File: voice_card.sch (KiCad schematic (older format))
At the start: 213 parts, among them J1 DDR3-DIMM, Q1 MMBF4391LT1G, Q10 DMMT3906, Q11 BC857BS, Q2 2N3904, Q3 BCM847, Q4 DMMT3904, Q5 DMMT3906, Q6 MMBF4391LT1G, Q7 BCM847, Q8 2N3904, Q9 DMMT3904, U1 TL074-, U10 TL072-, U11 TL074-, U12 NE555, U13 LM311M, U14 CD4052, U15 TL072-, U16 TL072-, U17 LM13700, U18 LM13700, U19 LM13700, U2 TL074-, U20 TL072-, U3 NE555, U4 LF351, U5 TL072-, U6 LM311M, U7 CD4052, U8 TL074-, U9 LF351

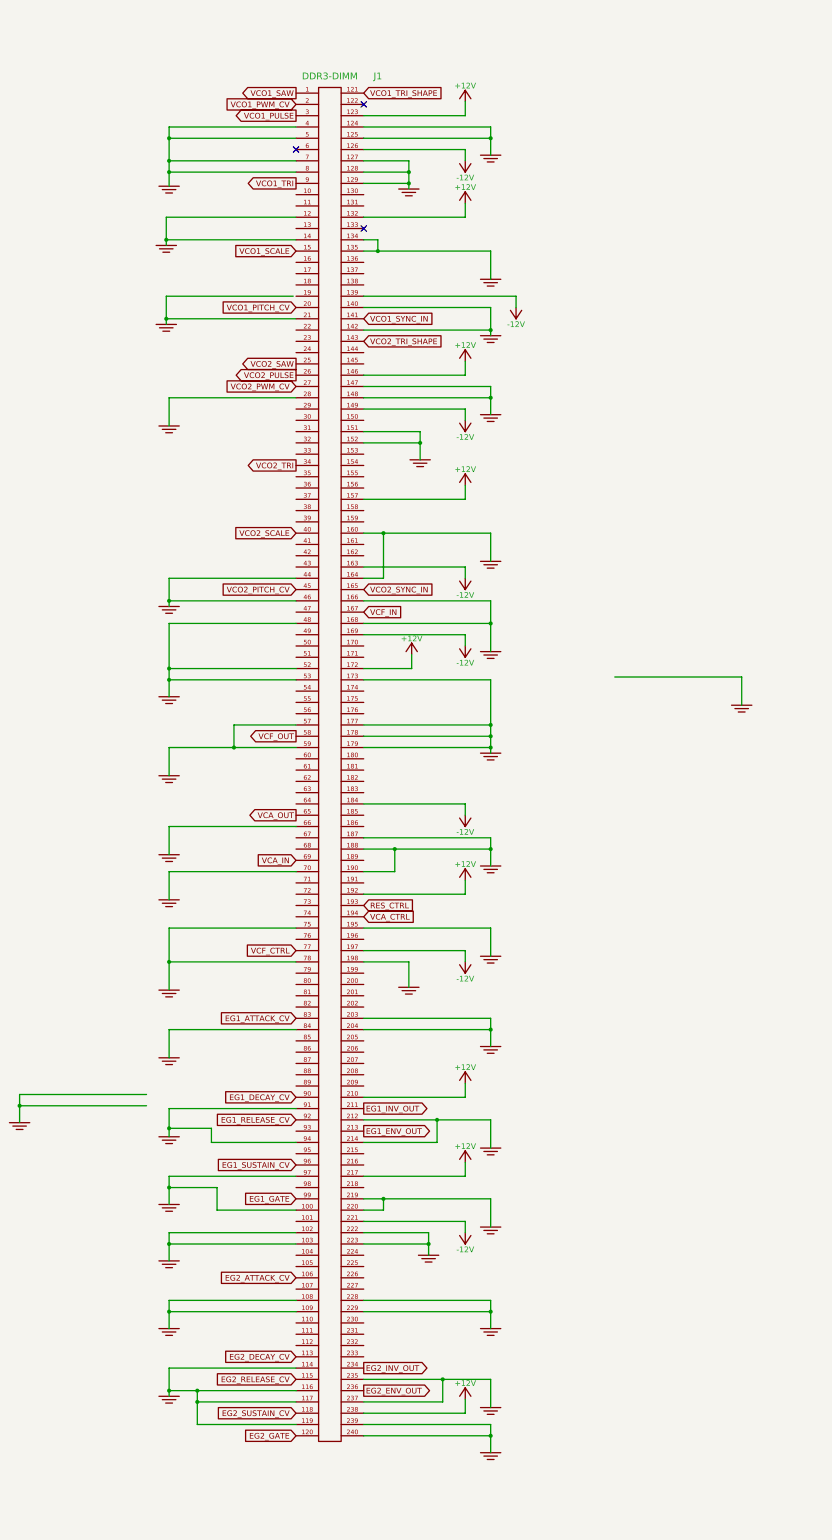
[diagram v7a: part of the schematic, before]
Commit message: made connections on DIMM socket bilaterally symmetrical and started to route accordingly
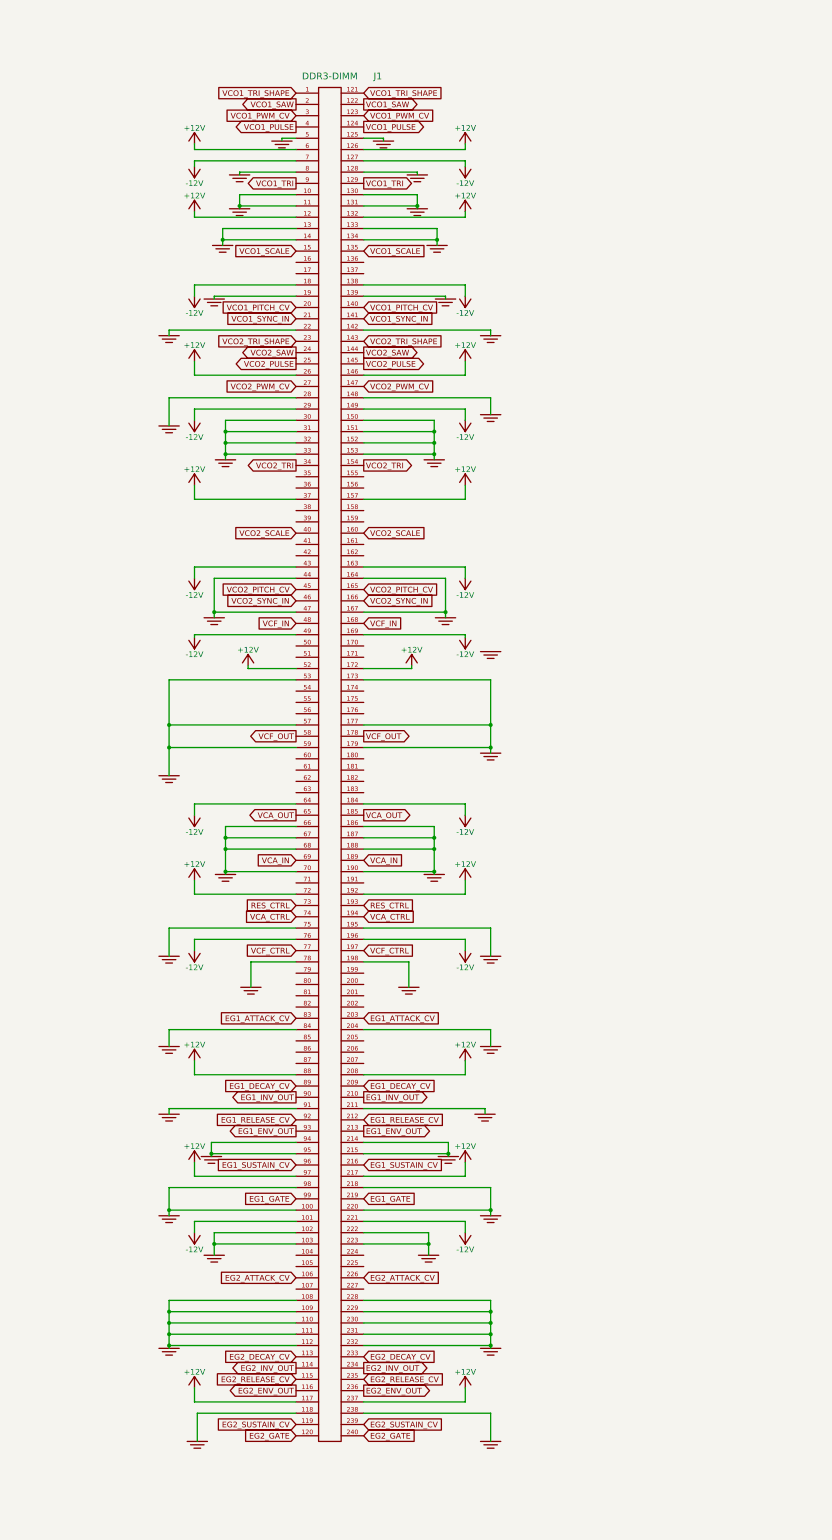
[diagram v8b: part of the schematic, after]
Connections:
- net +12V: now also J1.117, J1.12, J1.126, J1.208, J1.237, J1.26, J1.37, J1.52, J1.6, J1.72, J1.88, J1.97; no longer J1.123, J1.210, J1.238
- net -12V: now also J1.101, J1.127, J1.138, J1.18, J1.196, J1.29, J1.43, J1.49, J1.64, J1.7, J1.76; no longer J1.126, J1.139, J1.197
- net EG1_ATTACK_CV: now also J1.203
- net EG1_DECAY_CV: now also J1.209, J1.89; no longer J1.90
- net EG1_ENV_OUT: now also J1.93
- net EG1_GATE: now also J1.219
- net EG1_INV_OUT: now also J1.210, J1.90; no longer J1.211
- net EG1_RELEASE_CV: now also J1.212
- net EG1_SUSTAIN_CV: now also J1.216
- net EG2_ATTACK_CV: now also J1.226
- net EG2_DECAY_CV: now also J1.233
- net EG2_ENV_OUT: now also J1.116
- net EG2_GATE: now also J1.240
- net EG2_INV_OUT: now also J1.114
- net EG2_RELEASE_CV: now also J1.235
- net EG2_SUSTAIN_CV: now also J1.119, J1.239; no longer J1.118
- net GND: now also J1.10, J1.11, J1.110, J1.111, J1.112, J1.118, J1.13, J1.130, J1.131, J1.133, J1.139, J1.150, J1.153, J1.167, J1.186, J1.19, J1.211, J1.215, J1.218, J1.22, J1.230, J1.231, J1.232, J1.238, J1.30, J1.31, J1.32, J1.33, J1.47, J1.67, J1.68, J1.95, J1.98; no longer J1.114, J1.116, J1.117, J1.119, J1.12, J1.124, J1.127, J1.129, J1.135, J1.140, J1.147, J1.160, J1.166, J1.168, J1.178, J1.203, J1.21, J1.212, J1.219, J1.235, J1.237, J1.239, J1.240, J1.4, J1.46, J1.48, J1.52, J1.7, J1.97
- net RES_CTRL: now also J1.73
- net VCA_CTRL: now also J1.74
- net VCA_IN: now also J1.189
- net VCA_OUT: now also J1.185
- net VCF_CTRL: now also J1.197
- net VCF_IN: now also J1.168, J1.48; no longer J1.167
- net VCF_OUT: now also J1.178
- net VCO1_PITCH_CV: now also J1.140
- net VCO1_PULSE: now also J1.124, J1.4; no longer J1.3
- net VCO1_PWM_CV: now also J1.123, J1.3; no longer J1.2
- net VCO1_SAW: now also J1.122, J1.2; no longer J1.1
- net VCO1_SCALE: now also J1.135
- net VCO1_SYNC_IN: now also J1.21
- net VCO1_TRI: now also J1.129
- net VCO1_TRI_SHAPE: now also J1.1
- net VCO2_PITCH_CV: now also J1.165
- net VCO2_PULSE: now also J1.145, J1.25; no longer J1.26
- net VCO2_PWM_CV: now also J1.147
- net VCO2_SAW: now also J1.144, J1.24; no longer J1.25
- net VCO2_SCALE: now also J1.160
- net VCO2_SYNC_IN: now also J1.166, J1.46; no longer J1.165
- net VCO2_TRI: now also J1.154
- net VCO2_TRI_SHAPE: now also J1.23
- no-connect marks 11 -> 8
